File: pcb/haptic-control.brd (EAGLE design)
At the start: 40 x 160 mm, 148 parts, among them M1 SPH0641LM4H-1, P1 2P-PAD_1X3.5, P2 2P-PAD_1X3.5, P3 2P-PAD_1X3.5, P4 2P-PAD_1X3.5, U1 MIC23159, U10 DRV2605L, U11 DRV2605L, U12 MTCH6301, U2 BQ51050B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

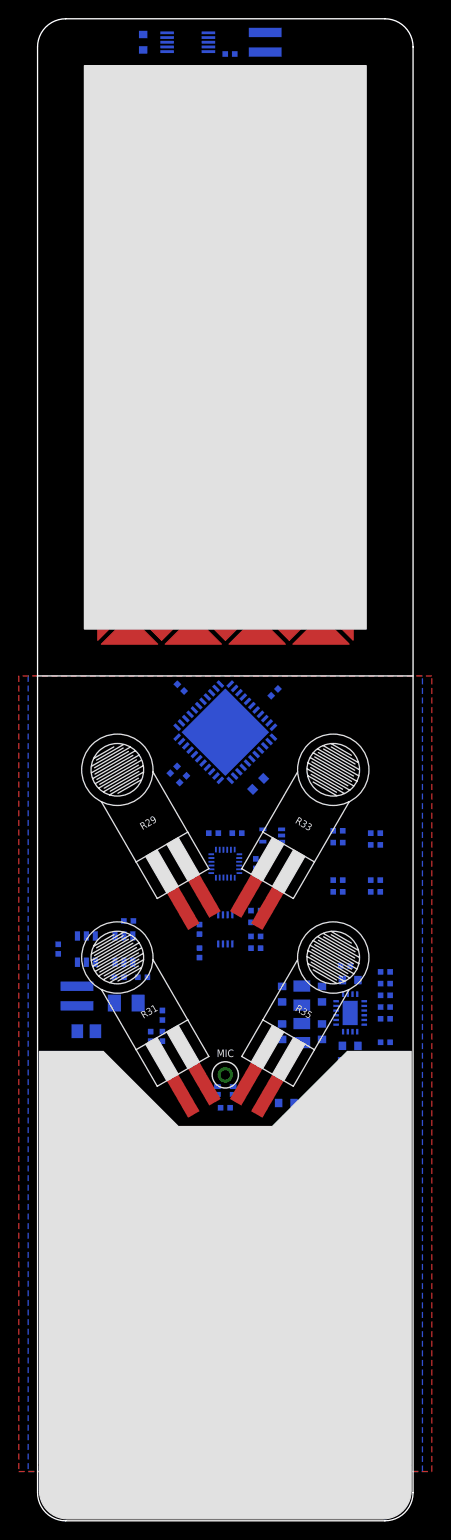
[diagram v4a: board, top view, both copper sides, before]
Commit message: touch matrix connections
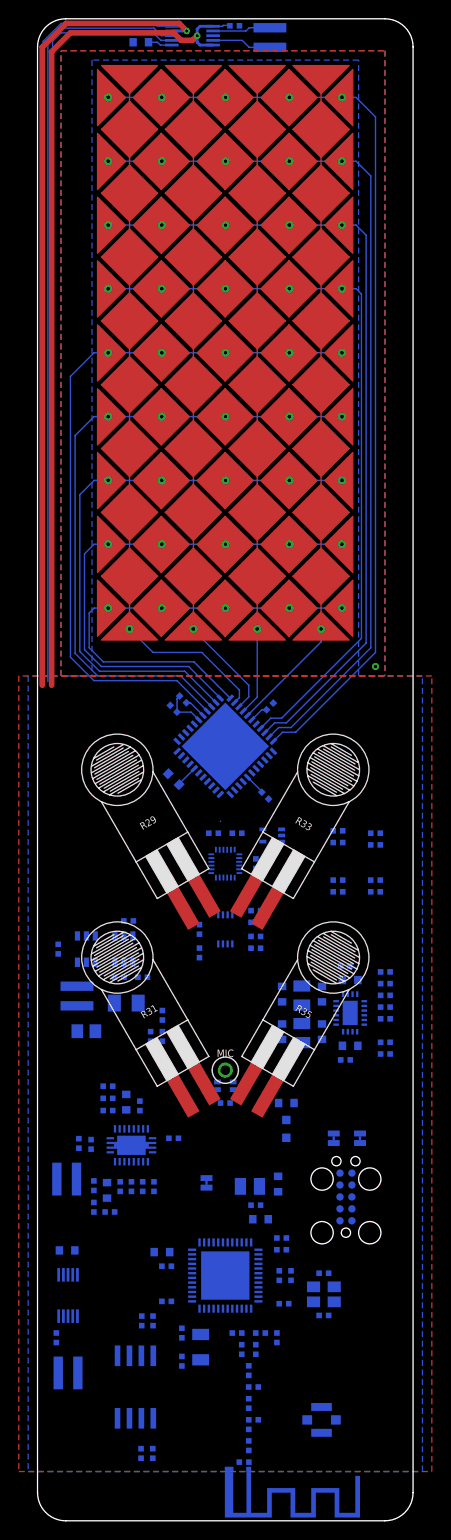
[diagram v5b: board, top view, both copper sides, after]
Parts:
- moved MAT-Y9 54.9 mm to (20.0, 151.6), turned to 180 degrees
- moved MAT-Y1 54.0 mm to (20.0, 97.2), turned to 180 degrees
- moved MAT-Y8 41.3 mm to (20.0, 144.8), turned to 180 degrees
- moved MAT-Y2 40.4 mm to (20.0, 104.0), turned to 180 degrees
- moved LOGO1 37.8 mm to (2.00, 69.5), turned to 90 degrees
- moved MAT-Y7 27.7 mm to (20.0, 138.0), turned to 180 degrees
- moved MAT-Y3 26.8 mm to (20.0, 110.8), turned to 180 degrees
- moved MAT-X1 20.4 mm to (30.2, 124.4), turned to 180 degrees
- moved MAT-X4 20.4 mm to (9.80, 124.4), turned to 180 degrees
- moved MAT-Y6 14.1 mm to (20.0, 131.2), turned to 180 degrees
- moved MAT-Y4 13.2 mm to (20.0, 117.6), turned to 180 degrees
- moved C57 11.0 mm to (24.2, 77.2), turned to 225 degrees
- moved C58 9.71 mm to (24.8, 86.8), turned to 135 degrees
- moved C60 9.01 mm to (14.5, 79.0), turned to 45 degrees
- moved C59 7.57 mm to (14.5, 86.5), turned to 45 degrees
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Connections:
- net 3.3V: now also R29.2, R31.2; no longer R29.1, R31.1
- net FSR_CH_N: now also R31.1; no longer R31.2
- net FSR_CH_P: now also R29.1; no longer R29.2
- net PCAP_RX0: now also MAT-X1.P$2
- net PCAP_RX1: now also MAT-X2.P$2
- net PCAP_RX2: now also MAT-X3.P$2
- net PCAP_RX3: now also MAT-X4.P$2
- net PCAP_RX4: now also MAT-Y1.P$2, MAT-Y1.P$3, MAT-Y1.P$4, MAT-Y1.P$5, MAT-Y1.P$8
- net PCAP_RX5: now also MAT-Y2.P$2, MAT-Y2.P$3, MAT-Y2.P$4, MAT-Y2.P$5, MAT-Y2.P$8
- net PCAP_RX6: now also MAT-Y3.P$2, MAT-Y3.P$3, MAT-Y3.P$4, MAT-Y3.P$5, MAT-Y3.P$8
- net PCAP_RX7: now also MAT-Y4.P$2, MAT-Y4.P$3, MAT-Y4.P$4, MAT-Y4.P$5, MAT-Y4.P$8
- net PCAP_RX8: now also MAT-Y5.P$2, MAT-Y5.P$3, MAT-Y5.P$4, MAT-Y5.P$5, MAT-Y5.P$8
- net PCAP_TX0: now also MAT-Y9.P$2, MAT-Y9.P$3, MAT-Y9.P$4, MAT-Y9.P$5, MAT-Y9.P$8
- net PCAP_TX1: now also MAT-Y8.P$2, MAT-Y8.P$3, MAT-Y8.P$4, MAT-Y8.P$5, MAT-Y8.P$8
- net PCAP_TX2: now also MAT-Y7.P$2, MAT-Y7.P$3, MAT-Y7.P$4, MAT-Y7.P$5, MAT-Y7.P$8
- net PCAP_TX3: now also MAT-Y6.P$2, MAT-Y6.P$3, MAT-Y6.P$4, MAT-Y6.P$5, MAT-Y6.P$8
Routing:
- net PCAP_TX0: track 0.00 -> 101.2 mm
- net PCAP_TX1: track 0.00 -> 93.6 mm
- net VBAT: track 0.00 -> 91.8 mm, vias 0 -> 1
- net GND: track 0.00 -> 86.3 mm, vias 0 -> 2
- net PCAP_TX2: track 0.00 -> 86.1 mm
- net LRA_EN: track 0.00 -> 82.8 mm
- net SDA: track 0.00 -> 82.4 mm
- net SCL: track 0.00 -> 81.7 mm
- net PCAP_TX3: track 0.00 -> 78.6 mm
- net PCAP_RX8: track 0.00 -> 76.8 mm
- net PCAP_RX7: track 0.00 -> 69.4 mm
- net PCAP_RX6: track 0.00 -> 62.0 mm
- net PCAP_RX5: track 0.00 -> 54.7 mm
- net PCAP_RX4: track 0.00 -> 48.1 mm
- net PCAP_RX3: track 0.00 -> 15.9 mm
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
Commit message: touch matrix gnd plane minor change
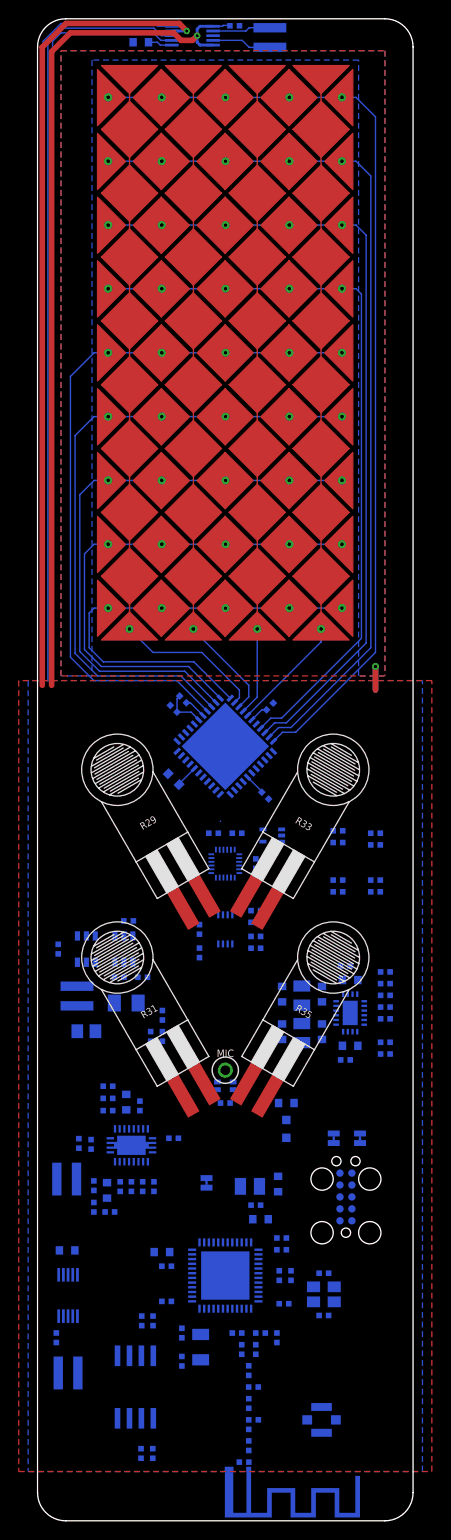
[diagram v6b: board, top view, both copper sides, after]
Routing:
- net GND: track 86.3 -> 91.3 mm
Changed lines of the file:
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@@
 <drawing>
 <settings>
-<setting alwaysvectorfont="yes"/>
+<setting alwaysvectorfont="no"/>
 <setting verticaltext="up"/>
 </settings>
@@
 <contactref element="M1" pad="2"/>
 <contactref element="C48" pad="2"/>
-<polygon width="0.2" layer="16" pour="cutout" locked="yes">
-<vertex x="41" y="90"/>
-<vertex x="-1" y="90"/>
+<polygon width="0.2" layer="16" pour="cutout">
+<vertex x="41" y="89.5"/>
+<vertex x="-1" y="89.5"/>
 <vertex x="-1" y="5.25"/>
 <vertex x="41" y="5.25"/>
 </polygon>
-<polygon width="0.2" layer="1" pour="cutout" isolate="0.2" locked="yes">
-<vertex x="42" y="90"/>
-<vertex x="-2" y="90"/>
+<polygon width="0.2" layer="1" pour="cutout" isolate="0.2">
+<vertex x="42" y="89.5"/>
+<vertex x="-2" y="89.5"/>
 <vertex x="-2" y="5.25"/>
 <vertex x="42" y="5.25"/>
@@
 <wire x1="3.0281375" y1="159.5" x2="0.5" y2="156.9718625" width="0.6" layer="1" locked="yes"/>
 <wire x1="0.5" y1="156.9718625" x2="0.5" y2="89" width="0.6" layer="1" locked="yes"/>
+<wire x1="36" y1="91" x2="36" y2="88.5" width="0.6096" layer="1"/>
+<wire x1="36" y1="91" x2="36" y2="88.5" width="0.6096" layer="16"/>
 <wire x1="18.7" y1="158.2" x2="21.508" y2="159.25" width="0" layer="19" extent="16-16"/>
 <wire x1="15.896625" y1="158.7" x2="18.7" y2="158.2" width="0" layer="19" extent="16-16"/>
@@
 <wire x1="20.4" y1="5.5" x2="21.492" y2="6.25" width="0" layer="19" extent="16-16"/>
 <wire x1="8.52" y1="10.92" x2="15.375" y2="17.508" width="0" layer="19" extent="16-16"/>
-<wire x1="36" y1="91" x2="25.1092125" y2="87.109209375" width="0" layer="19" extent="16-16"/>
+<wire x1="36" y1="88.5" x2="25.1092125" y2="87.109209375" width="0" layer="19" extent="1-16"/>
 </signal>
 <signal name="XTAL_48M_N">

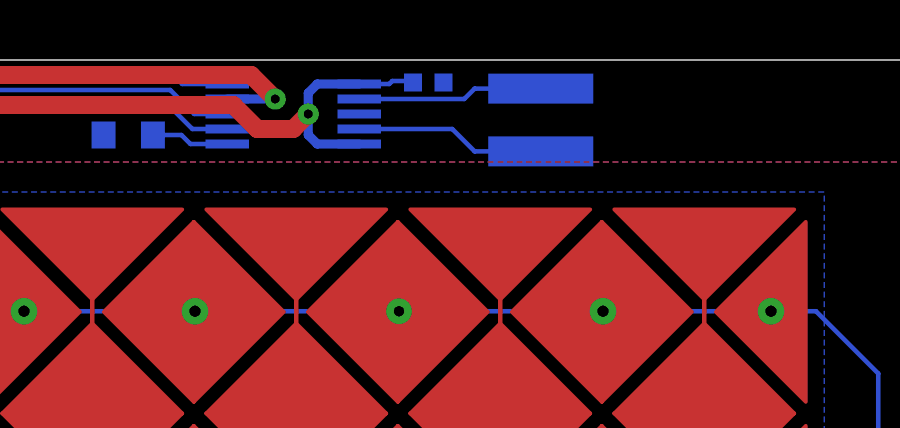
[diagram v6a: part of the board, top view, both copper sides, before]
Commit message: i2c level shifter sch fix
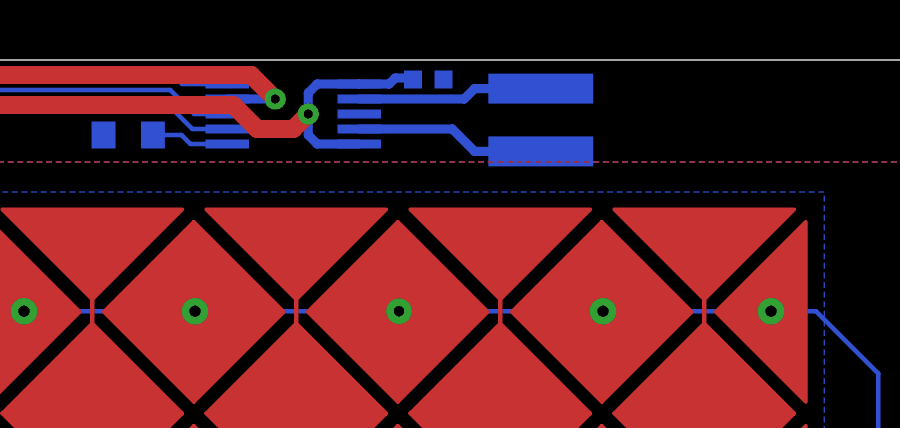
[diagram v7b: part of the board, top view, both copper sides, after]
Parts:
- moved C53 0.10 mm to (21.0, 159.3)
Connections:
- net MPU_PWR: now also U9.8
- net N$11: no longer U9.8
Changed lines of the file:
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@@
 <wire x1="-2" y1="50" x2="42" y2="50" width="0.127" layer="49" locked="yes"/>
 <circle x="35" y="155" locked="yes" radius="4" width="0.127" layer="49"/>
-<circle x="5" y="5" radius="4" width="0.127" layer="49"/>
-<text x="5" y="5" size="1.5" layer="49" align="center">LRA</text>
+<circle x="5" y="5" locked="yes" radius="4" width="0.127" layer="49"/>
+<text x="5" y="5" locked="yes" size="1.5" layer="49" align="center">LRA</text>
 <text x="35" y="155" locked="yes" size="1.5" layer="49" align="center">LRA</text>
 <circle x="8.5" y="80" locked="yes" radius="4.5" width="0.127" layer="49"/>
@@
 <attribute name="NAME" x="9.4275" y="53.1387" size="0.762" layer="26" font="vector" ratio="10" rot="MR180" align="center"/>
 </element>
-<element name="U$1" library="Eletromechanical &gt; LRAs" package="G0825001" value="" x="5" y="5" smashed="yes" rot="MR170"/>
+<element name="U$1" library="Eletromechanical &gt; LRAs" package="G0825001" value="" x="5" y="5" locked="yes" smashed="yes" rot="MR170"/>
 <element name="U$2" library="Eletromechanical &gt; LRAs" package="G0825001" value="" x="35" y="155" locked="yes" smashed="yes" rot="MR102.5"/>
 <element name="P3" library="Connectors &gt; Other" package="PAD1X3_5MM-2P" value="2P-PAD_1X3.5" x="3.25" y="15.75" smashed="yes" rot="MR0">
@@
 <attribute name="NAME" x="1.0061" y="19.4525" size="0.762" layer="26" font="vector" ratio="10" rot="MR270" align="center"/>
 </element>
-<element name="C53" library="Passive Components &gt; Capacitors &gt; Multilayer Ceramic Capacitors MLCC" package="_0402" value="100n" x="21" y="159.25" locked="yes" smashed="yes" rot="MR180">
+<element name="C53" library="Passive Components &gt; Capacitors &gt; Multilayer Ceramic Capacitors MLCC" package="_0402" value="100n" x="21" y="159.35" locked="yes" smashed="yes" rot="MR180">
 <attribute name="NAME" x="21.0475" y="158.2561" locked="yes" size="0.762" layer="26" font="vector" ratio="10" rot="MR180" align="center"/>
 </element>
@@
 <contactref element="U2" pad="25@5"/>
 <contactref element="U2" pad="25@1"/>
-<polygon width="0.1524" layer="16" isolate="0.3">
+<polygon width="0.1524" layer="16" isolate="0.3" locked="yes">
 <vertex x="2.5" y="90"/>
 <vertex x="2.5" y="156.6"/>
@@
 <wire x1="36" y1="91" x2="36" y2="88.5" width="0.6096" layer="1"/>
 <wire x1="36" y1="91" x2="36" y2="88.5" width="0.6096" layer="16"/>
-<wire x1="18.7" y1="158.2" x2="21.508" y2="159.25" width="0" layer="19" extent="16-16"/>
+<wire x1="18.7" y1="158.2" x2="21.508" y2="159.35" width="0" layer="19" extent="16-16"/>
 <wire x1="15.896625" y1="158.7" x2="18.7" y2="158.2" width="0" layer="19" extent="16-16"/>
 <wire x1="10.177" y1="157.5" x2="14.3" y2="158.7" width="0" layer="19" extent="16-16"/>
@@
 </signal>
 <signal name="N$11">
-<contactref element="U9" pad="8"/>
 <contactref element="U9" pad="7"/>
 <contactref element="R28" pad="1"/>
 <contactref element="C48" pad="1"/>
-<wire x1="19.75" y1="61.45" x2="19.25" y2="61.45" width="0" layer="19" extent="16-16"/>
-<wire x1="17.25" y1="61.008" x2="19.25" y2="61.45" width="0" layer="19" extent="16-16"/>
+<wire x1="17.25" y1="61.008" x2="19.75" y2="61.45" width="0" layer="19" extent="16-16"/>
 <wire x1="17.25" y1="62.492" x2="17.25" y2="61.008" width="0" layer="19" extent="16-16"/>
 </signal>
@@
 <contactref element="C19" pad="P$1"/>
 <wire x1="18.7" y1="159.2" x2="18.2" y2="159.2" width="0.1524" layer="16" locked="yes"/>
-<wire x1="18.7" y1="159.2" x2="19.7" y2="159.2" width="0.1524" layer="16" locked="yes"/>
-<wire x1="19.7" y1="159.2" x2="19.8" y2="159.3" width="0.1524" layer="16" locked="yes"/>
-<wire x1="19.8" y1="159.3" x2="20.442" y2="159.3" width="0.1524" layer="16" locked="yes"/>
 <wire x1="20.442" y1="159.3" x2="20.492" y2="159.25" width="0.1524" layer="16" locked="yes"/>
 <wire x1="18.7" y1="159.2" x2="17.3" y2="159.2" width="0.3048" layer="16" locked="yes"/>
@@
 <wire x1="3.5" y1="158.5" x2="1.5" y2="156.5" width="0.6" layer="1" locked="yes"/>
 <wire x1="1.5" y1="156.5" x2="1.5" y2="89" width="0.6" layer="1" locked="yes"/>
-<wire x1="32.477" y1="57.6" x2="32.292" y2="59.1" width="0" layer="19" extent="16-16"/>
-<wire x1="32.55" y1="56.1" x2="32.477" y2="57.6" width="0" layer="19" extent="16-16"/>
-<wire x1="31.8" y1="55.35" x2="32.55" y2="56.1" width="0" layer="19" extent="16-16"/>
-<wire x1="30.3" y1="55.277" x2="31.8" y2="55.35" width="0" layer="19" extent="16-16"/>
+<wire x1="18.7" y1="159.2" x2="19.7" y2="159.2" width="0.3048" layer="16" locked="yes"/>
+<wire x1="19.7" y1="159.2" x2="19.9" y2="159.4" width="0.3048" layer="16" locked="yes"/>
+<wire x1="19.9" y1="159.4" x2="20.442" y2="159.4" width="0.3048" layer="16" locked="yes"/>
+<wire x1="20.442" y1="159.4" x2="20.492" y2="159.35" width="0.3048" layer="16"/>
+<wire x1="20.492" y1="159.35" x2="20.442" y2="159.3" width="0" layer="19" extent="16-16"/>
+<wire x1="11.708" y1="57.9" x2="1.5" y2="89" width="0" layer="19" extent="1-16"/>
+<wire x1="13.3" y1="54.358" x2="11.708" y2="57.9" width="0" layer="19" extent="16-16"/>
+<wire x1="8.18" y1="55.15" x2="11.708" y2="57.9" width="0" layer="19" extent="16-16"/>
+<wire x1="6.1652" y1="52.15" x2="8.18" y2="55.15" width="0" layer="19" extent="16-16"/>
+<wire x1="9.45" y1="43.777" x2="6.1652" y2="52.15" width="0" layer="19" extent="16-16"/>
+<wire x1="9.25" y1="41.75" x2="9.45" y2="43.777" width="0" layer="19" extent="16-16"/>
+<wire x1="30.3" y1="55.277" x2="13.3" y2="54.358" width="0" layer="19" extent="16-16"/>
+<wire x1="31.8" y1="55.35" x2="30.3" y2="55.277" width="0" layer="19" extent="16-16"/>
+<wire x1="32.55" y1="56.1" x2="31.8" y2="55.35" width="0" layer="19" extent="16-16"/>
+<wire x1="32.477" y1="57.6" x2="32.55" y2="56.1" width="0" layer="19" extent="16-16"/>
+<wire x1="32.292" y1="59.1" x2="32.477" y2="57.6" width="0" layer="19" extent="16-16"/>
 <wire x1="30.3" y1="52.923" x2="30.3" y2="55.277" width="0" layer="19" extent="16-16"/>
 <wire x1="31.8" y1="52.85" x2="30.3" y2="52.923" width="0" layer="19" extent="16-16"/>
@@
 <wire x1="32.477" y1="50.6" x2="32.55" y2="52.1" width="0" layer="19" extent="16-16"/>
 <wire x1="32.292" y1="49.1" x2="32.477" y2="50.6" width="0" layer="19" extent="16-16"/>
-<wire x1="13.3" y1="54.358" x2="30.3" y2="55.277" width="0" layer="19" extent="16-16"/>
-<wire x1="11.708" y1="57.9" x2="13.3" y2="54.358" width="0" layer="19" extent="16-16"/>
-<wire x1="8.18" y1="55.15" x2="11.708" y2="57.9" width="0" layer="19" extent="16-16"/>
-<wire x1="6.1652" y1="52.15" x2="8.18" y2="55.15" width="0" layer="19" extent="16-16"/>
-<wire x1="9.45" y1="43.777" x2="6.1652" y2="52.15" width="0" layer="19" extent="16-16"/>
-<wire x1="9.25" y1="41.75" x2="9.45" y2="43.777" width="0" layer="19" extent="16-16"/>
 <wire x1="4.25" y1="21.8" x2="9.25" y2="41.75" width="0" layer="19" extent="16-16"/>
 <wire x1="2.25" y1="21.8" x2="4.25" y2="21.8" width="0" layer="19" extent="16-16"/>
 <wire x1="2" y1="20.008" x2="2.25" y2="21.8" width="0" layer="19" extent="16-16"/>
-<wire x1="1.5" y1="89" x2="11.708" y2="57.9" width="0" layer="19" extent="1-16"/>
 </signal>
 <signal name="GBAT">
@@
 <contactref element="U1" pad="9"/>
 <contactref element="U5" pad="21"/>
+<contactref element="U9" pad="8"/>
 <wire x1="33.55" y1="56.1" x2="33.308" y2="59.1" width="0" layer="19" extent="16-16"/>
+<wire x1="19.25" y1="61.45" x2="33.308" y2="59.1" width="0" layer="19" extent="16-16"/>
 <wire x1="16.47" y1="27.375" x2="33.55" y2="56.1" width="0" layer="19" extent="16-16"/>
 </signal>
@@
 <contactref element="U11" pad="7"/>
 <contactref element="P4" pad="1"/>
-<wire x1="18.7" y1="158.7" x2="22.2" y2="158.7" width="0.1524" layer="16" locked="yes"/>
-<wire x1="22.546" y1="159.046" x2="24.75" y2="159.046" width="0.1524" layer="16" locked="yes"/>
-<wire x1="22.2" y1="158.7" x2="22.546" y2="159.046" width="0.1524" layer="16" locked="yes"/>
+<wire x1="18.7" y1="158.7" x2="22.2" y2="158.7" width="0.3048" layer="16" locked="yes"/>
+<wire x1="22.546" y1="159.046" x2="24.75" y2="159.046" width="0.3048" layer="16" locked="yes"/>
+<wire x1="22.2" y1="158.7" x2="22.546" y2="159.046" width="0.3048" layer="16" locked="yes"/>
 </signal>
 <signal name="N$35">
 <contactref element="U11" pad="9"/>
 <contactref element="P4" pad="2"/>
-<wire x1="18.7" y1="157.7" x2="21.8" y2="157.7" width="0.1524" layer="16" locked="yes"/>
-<wire x1="22.546" y1="156.954" x2="24.75" y2="156.954" width="0.1524" layer="16" locked="yes"/>
-<wire x1="21.8" y1="157.7" x2="22.546" y2="156.954" width="0.1524" layer="16" locked="yes"/>
+<wire x1="18.7" y1="157.7" x2="21.8" y2="157.7" width="0.3048" layer="16" locked="yes"/>
+<wire x1="22.546" y1="156.954" x2="24.75" y2="156.954" width="0.3048" layer="16" locked="yes"/>
+<wire x1="21.8" y1="157.7" x2="22.546" y2="156.954" width="0.3048" layer="16" locked="yes"/>
 </signal>
 <signal name="N$36">

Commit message: removed hardware MPU pwr switch
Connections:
- net MPU_PWR: no longer U5.21, U9.8
- net N$11: now also U9.8
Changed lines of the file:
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@@
 <contactref element="R28" pad="1"/>
 <contactref element="C48" pad="1"/>
-<wire x1="17.25" y1="61.008" x2="19.75" y2="61.45" width="0" layer="19" extent="16-16"/>
+<contactref element="U9" pad="8"/>
+<wire x1="19.25" y1="61.45" x2="19.75" y2="61.45" width="0" layer="19" extent="16-16"/>
+<wire x1="17.25" y1="61.008" x2="19.25" y2="61.45" width="0" layer="19" extent="16-16"/>
 <wire x1="17.25" y1="62.492" x2="17.25" y2="61.008" width="0" layer="19" extent="16-16"/>
 </signal>
@@
 <contactref element="R5" pad="1"/>
 <contactref element="U1" pad="9"/>
-<contactref element="U5" pad="21"/>
-<contactref element="U9" pad="8"/>
 <wire x1="33.55" y1="56.1" x2="33.308" y2="59.1" width="0" layer="19" extent="16-16"/>
-<wire x1="19.25" y1="61.45" x2="33.308" y2="59.1" width="0" layer="19" extent="16-16"/>
-<wire x1="16.47" y1="27.375" x2="33.55" y2="56.1" width="0" layer="19" extent="16-16"/>
 </signal>
 <signal name="N$30">
